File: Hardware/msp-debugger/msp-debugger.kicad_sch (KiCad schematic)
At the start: 22 parts, among them J1 Conn_02x10, J1 USB_B_Micro, J2 Conn_02x10, J4 Conn_01x04_Pin, SW1 222ADVBA, SW2 222ADVBA, SW3 222ADVBA, SW4 222ADVBA, SW5 222ADVBA, U1 MSP430G2553IN20, U3 BA033CC0FP-E2, U4 FT230XS-R

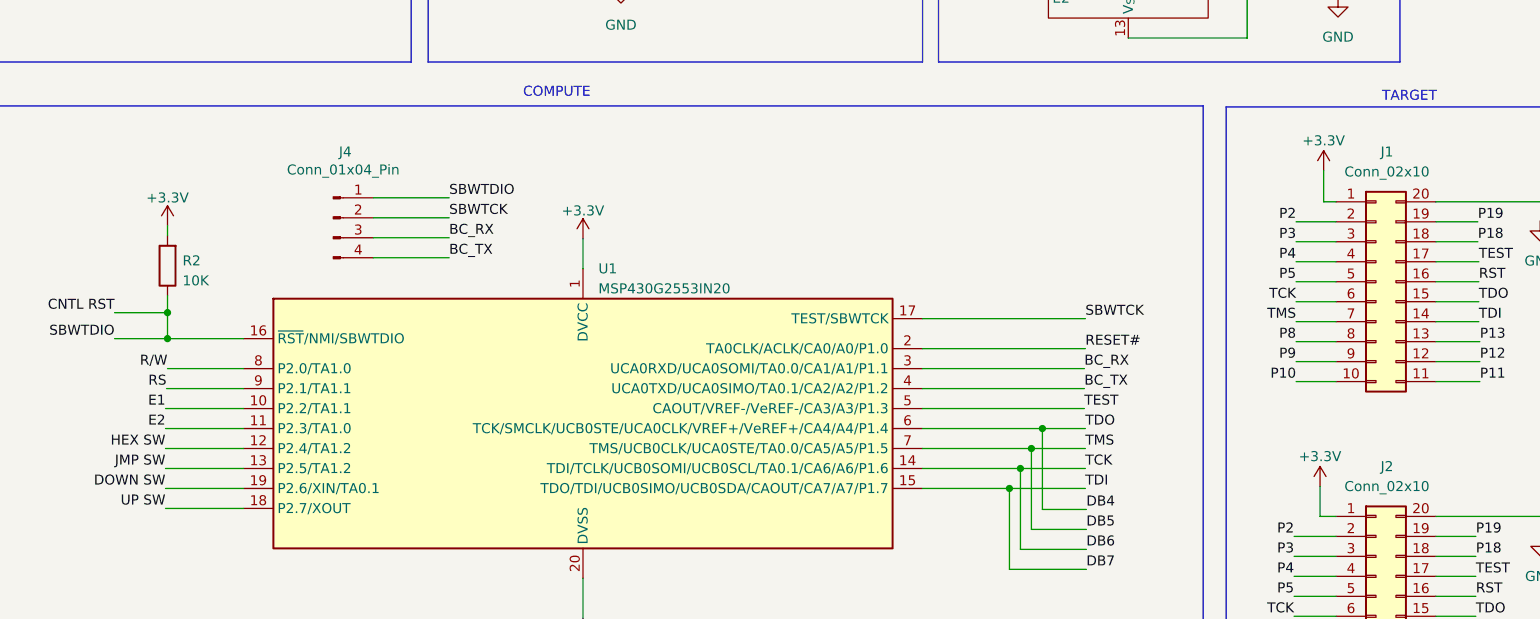
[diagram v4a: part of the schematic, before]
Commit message: reroute pcb for 40 line lcd screen
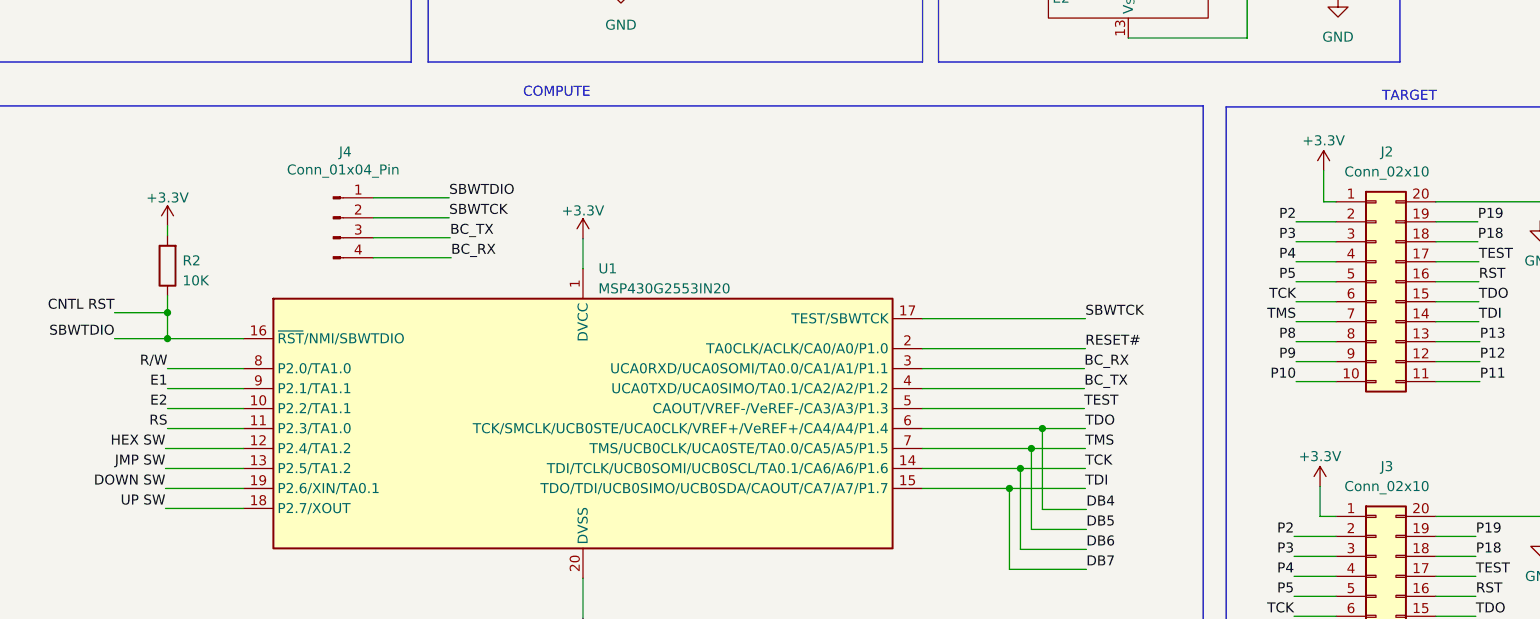
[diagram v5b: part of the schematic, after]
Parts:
- U2: footprint (none) -> project:NHD-0440AZ-FL-YBW
- VR1: footprint 3362P-1-103LF:TRIM_3362P-1-103LF -> project:TRIM_3362P-1-103LF
- renumbered J1 to J2, J2 to J3
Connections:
- net BC_RX: now also J4.4 (Pin_4); no longer J4.3 (Pin_3)
- net BC_TX: now also J4.3 (Pin_3); no longer J4.4 (Pin_4)
- net E1: now also U1.9 (P2.1/TA1.1); no longer U1.10 (P2.2/TA1.1)
- net E2: now also U1.10 (P2.2/TA1.1); no longer U1.11 (P2.3/TA1.0)
- net RS: now also U1.11 (P2.3/TA1.0); no longer U1.9 (P2.1/TA1.1)
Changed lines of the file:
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@@
+    (stroke (width 0) (type default))
+  )
+  (wire (pts (xy 124.968 101.6) (xy 134.874 101.6))
     (stroke (width 0) (type default))
   )
@@
     (stroke (width 0) (type default))
   )
-  (wire (pts (xy 124.968 99.06) (xy 134.62 99.06))
-    (stroke (width 0) (type default))
-  )
   (wire (pts (xy 233.68 64.77) (xy 236.093 64.77))
     (stroke (width 0) (type default))
@@
     (stroke (width 0) (type default))
   )
-  (wire (pts (xy 108.458 123.317) (xy 98.552 123.317))
-    (stroke (width 0) (type default))
-  )
   (wire (pts (xy 59.055 60.833) (xy 68.6054 60.833))
     (stroke (width 0) (type default))
@@
     (stroke (width 0) (type default))
   )
-  (wire (pts (xy 124.968 101.6) (xy 134.62 101.6))
-    (stroke (width 0) (type default))
-  )
   (wire (pts (xy 98.552 125.857) (xy 108.458 125.857))
     (stroke (width 0) (type default))
@@
     (stroke (width 0) (type default))
   )
+  (wire (pts (xy 108.458 120.777) (xy 98.806 120.777))
+    (stroke (width 0) (type default))
+  )
   (wire (pts (xy 54.483 109.601) (xy 56.388 109.601))
     (stroke (width 0) (type default))
   )
+  (wire (pts (xy 242.316 104.648) (xy 247.396 104.648))
+    (stroke (width 0) (type default))
+  )
   (wire (pts (xy 260.096 149.733) (xy 265.176 149.733))
     (stroke (width 0) (type default))
@@
     (stroke (width 0) (type default))
   )
+  (wire (pts (xy 98.806 118.237) (xy 108.458 118.237))
+    (stroke (width 0) (type default))
+  )
   (wire (pts (xy 203.0476 53.34) (xy 208.28 53.34))
     (stroke (width 0) (type default))
@@
     (stroke (width 0) (type default))
   )
-  (wire (pts (xy 242.316 104.648) (xy 247.396 104.648))
-    (stroke (width 0) (type default))
-  )
   (wire (pts (xy 151.638 142.367) (xy 151.638 147.447))
     (stroke (width 0) (type default))
@@
     (stroke (width 0) (type default))
   )
-  (wire (pts (xy 98.552 120.777) (xy 108.458 120.777))
-    (stroke (width 0) (type default))
-  )
   (wire (pts (xy 219.71 29.718) (xy 247.65 29.718))
     (stroke (width 0) (type default))
@@
     (stroke (width 0) (type default))
   )
-  (wire (pts (xy 98.679 118.237) (xy 108.458 118.237))
-    (stroke (width 0) (type default))
-  )
   (wire (pts (xy 42.418 119.126) (xy 44.323 119.126))
     (stroke (width 0) (type default))
@@
     (stroke (width 0) (type default))
   )
+  (wire (pts (xy 124.968 99.06) (xy 134.747 99.06))
+    (stroke (width 0) (type default))
+  )
   (wire (pts (xy 72.136 47.117) (xy 77.724 47.117))
     (stroke (width 0) (type default))
@@
     (stroke (width 0) (type default))
   )
+  (wire (pts (xy 108.458 123.317) (xy 98.806 123.317))
+    (stroke (width 0) (type default))
+  )
   (wire (pts (xy 37.973 119.126) (xy 42.418 119.126))
     (stroke (width 0) (type default))
@@
     (effects (font (size 1.27 1.27)) (justify right bottom))
   )
-  (label "E2" (at 98.552 123.317 180) (fields_autoplaced)
+  (label "E2" (at 98.806 120.777 180) (fields_autoplaced)
     (effects (font (size 1.27 1.27)) (justify right bottom))
   )
@@
     (effects (font (size 1.27 1.27)) (justify right bottom))
   )
-  (label "BC_RX" (at 134.62 99.06 0) (fields_autoplaced)
+  (label "BC_RX" (at 134.874 101.6 0) (fields_autoplaced)
     (effects (font (size 1.27 1.27)) (justify left bottom))
   )
@@
     (effects (font (size 1.27 1.27)) (justify left bottom))
   )
-  (label "E1" (at 98.552 120.777 180) (fields_autoplaced)
+  (label "E1" (at 98.806 118.237 180) (fields_autoplaced)
     (effects (font (size 1.27 1.27)) (justify right bottom))
   )
@@
     (effects (font (size 1.27 1.27)) (justify right bottom))
   )
-  (label "RS" (at 98.679 118.237 180) (fields_autoplaced)
+  (label "RS" (at 98.806 123.317 180) (fields_autoplaced)
     (effects (font (size 1.27 1.27)) (justify right bottom))
   )
@@
     (effects (font (size 1.27 1.27)) (justify left bottom))
   )
-  (label "BC_TX" (at 134.62 101.6 0) (fields_autoplaced)
+  (label "BC_TX" (at 134.747 99.06 0) (fields_autoplaced)
     (effects (font (size 1.27 1.27)) (justify left bottom))
   )
@@
       (effects (font (size 1.27 1.27)) (justify left))
     )
-    (property "Footprint" "3362P-1-103LF:TRIM_3362P-1-103LF" (at 247.65 39.878 0)
+    (property "Footprint" "project:TRIM_3362P-1-103LF" (at 247.65 39.878 0)
       (effects (font (size 1.27 1.27)) (justify bottom) hide)
     )
@@
   (symbol (lib_id "Connector_Generic:Conn_02x10_Counter_Clockwise") (at 252.476 104.648 0) (unit 1)
     (in_bom yes) (on_board yes) (dnp no)
-    (property "Reference" "J1" (at 253.873 88.138 0)
+    (property "Reference" "J2" (at 253.873 88.138 0)
       (effects (font (size 1.27 1.27)))
     )
@@
       (project "msp-debugger"
         (path "/045ba461-bcb4-4373-9dc5-687bfd2826ef"
-          (reference "J1") (unit 1)
+          (reference "J2") (unit 1)
         )
       )
@@
       (effects (font (size 1.27 1.27)))
     )
-    (property "Footprint" "" (at 220.98 46.99 0)
+    (property "Footprint" "project:NHD-0440AZ-FL-YBW" (at 220.98 46.99 0)
       (effects (font (size 1.27 1.27)) hide)
     )
@@
   (symbol (lib_id "Connector_Generic:Conn_02x10_Counter_Clockwise") (at 252.476 144.653 0) (unit 1)
     (in_bom yes) (on_board yes) (dnp no)
-    (property "Reference" "J2" (at 253.873 128.143 0)
+    (property "Reference" "J3" (at 253.873 128.143 0)
       (effects (font (size 1.27 1.27)))
     )
@@
       (project "msp-debugger"
         (path "/045ba461-bcb4-4373-9dc5-687bfd2826ef"
-          (reference "J2") (unit 1)
-        )
-      )
+          (reference "J3") (unit 1)
+        )
+      )

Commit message: fix hardware issues and route small pcb
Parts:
- removed J3: Conn_02x10, Connector_PinHeader_2.54mm:PinHeader_2x10_P2.54mm_Vertical, symbol Connector_Generic:Conn_02x10_Counter_Clockwise
- removed J4: Conn_01x04_Pin, Connector_PinHeader_2.54mm:PinHeader_1x04_P2.54mm_Vertical, symbol Connector:Conn_01x04_Pin
- removed U4: FT230XS-R, digikey-footprints:SOIC-16_W3.90mm, symbol dk_Interface-Controllers:FT230XS-R
- added J4: MSP_FET PORT, Connector_PinHeader_2.54mm:PinHeader_2x03_P2.54mm_Vertical, symbol Connector_Generic:Conn_02x03_Counter_Clockwise
- added J5: USB JUMPER, Connector_PinHeader_2.54mm:PinHeader_2x03_P2.54mm_Vertical, symbol Connector_Generic:Conn_02x03_Counter_Clockwise
- added J6, J7: Conn_01x10, Connector_PinHeader_2.54mm:PinHeader_1x10_P2.54mm_Vertical, symbol Connector_Generic:Conn_01x10
- added R10, R3, R4, R5, R6, R7, R8, R9: 10K, Capacitor_SMD:C_0805_2012Metric, symbol Device:R
- added SW6: 222ADVBA, buttons:SW_222ADVBA, symbol Switch:SW_MEC_5E
- added U4: FT230XS-R, SOIC_30XS-R_FTD, symbol ft230xs-r:FT230XS-R
- added U5, U6, U7, U8: AO4882, SO-8_AOS, symbol ao4882:AO4882
- J1: footprint Connector_USB:USB_Micro-B_Amphenol_10118194_Horizontal -> Connector_PinHeader_2.54mm:PinHeader_1x05_P2.54mm_Vertical
- U2: footprint project:NHD-0440AZ-FL-YBW -> Connector_PinHeader_2.54mm:PinHeader_2x09_P2.54mm_Vertical
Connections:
- net RST is gone; now on net DB7: J2.16 (Pin_16)
- net +3.3V: now also J6.1 (Pin_1), U4.3 (VCCIO)
- net +5V: now also U4.12 (VCC), U5.5 (D1), U5.6 (D1), U5.7 (D2), U5.8 (D2), U6.5 (D1), U6.6 (D1), U6.7 (D2), U6.8 (D2), U7.5 (D1), U7.6 (D1), U7.7 (D2), U7.8 (D2), U8.5 (D1), U8.6 (D1), U8.7 (D2), U8.8 (D2)
- net BC_RX: now also J4.5 (Pin_5), J5.5 (Pin_5)
- net BC_TX: now also J4.6 (Pin_6), J5.4 (Pin_4)
- net CNTL RST: now also J4.3 (Pin_3)
- net D+: now also U4.8 (USBDP)
- net D-: now also U4.9 (USBDM)
- net DB4: now also J2.14 (Pin_14), U1.7 (TMS/UCB0CLK/UCA0STE/TA0.0/CA5/A5/P1.5), J7.4 (Pin_4), U5.4 (G1); no longer J2.15 (Pin_15), U1.6 (TCK/SMCLK/UCB0STE/UCA0CLK/VREF+/VeREF+/CA4/A4/P1.4), U2.4 (DB4)
- net DB5: now also J2.17 (Pin_17), U1.2 (TA0CLK/ACLK/CA0/A0/P1.0), J7.7 (Pin_7), U6.2 (G2); no longer J2.7 (Pin_7), U1.7 (TMS/UCB0CLK/UCA0STE/TA0.0/CA5/A5/P1.5), U2.3 (DB5)
- net DB6: now also J2.15 (Pin_15), U1.6 (TCK/SMCLK/UCB0STE/UCA0CLK/VREF+/VeREF+/CA4/A4/P1.4), J7.5 (Pin_5), U5.2 (G2); no longer J2.6 (Pin_6), U1.14 (TDI/TCLK/UCB0SOMI/UCB0SCL/TA0.1/CA6/A6/P1.6), U2.2 (DB6)
- net DB7: now also U1.5 (CAOUT/VREF-/VeREF-/CA3/A3/P1.3), J7.6 (Pin_6), U6.4 (G1); no longer J2.14 (Pin_14), U1.15 (TDO/TDI/UCB0SIMO/UCB0SDA/CAOUT/CA7/A7/P1.7), U2.1 (DB7)
- net DOWN SW: now also U1.18 (P2.7/XOUT); no longer U1.19 (P2.6/XIN/TA0.1)
- net E1: now also U1.11 (P2.3/TA1.0), U7.4 (G1); no longer U1.9 (P2.1/TA1.1), U2.9 (E1)
- net E2: now also U1.9 (P2.1/TA1.1), U8.4 (G1); no longer U1.10 (P2.2/TA1.1), U2.15 (E2)
- net GND: now also J4.2 (Pin_2), J7.10 (Pin_10), R10.1, R3.1, R4.1, R5.1, R6.1, R7.1, R8.1, R9.1, SW6.1, SW6.2, U4.13 (GND), U4.5 (GND)
- net P10: now also J6.10 (Pin_10)
- net P11: now also J7.1 (Pin_1)
- net P12: now also J7.2 (Pin_2)
- net P13: now also J7.3 (Pin_3)
- net P18: now also J7.8 (Pin_8)
- net P19: now also J7.9 (Pin_9)
- net P2: now also J6.2 (Pin_2)
- net P3: now also J6.3 (Pin_3)
- net P4: now also J6.4 (Pin_4)
- net P5: now also J6.5 (Pin_5)
- net P8: now also J6.8 (Pin_8)
- net P9: now also J6.9 (Pin_9)
- net RESET#: now also SW6.3 (K), SW6.4 (A), U4.11 (RESET#); no longer U1.2 (TA0CLK/ACLK/CA0/A0/P1.0)
- net RS: now also U1.10 (P2.2/TA1.1), U7.2 (G2); no longer U1.11 (P2.3/TA1.0), U2.11 (RS)
- net R/W: now also U8.2 (G2); no longer U2.10 (R/W)
- net SBWTCK: now also J4.4 (Pin_4)
- net UP SW: now also U1.19 (P2.6/XIN/TA0.1); no longer U1.18 (P2.7/XOUT)
- net PWR_IN: now reaches F1.1
- net PWR_IN: now also J4.1 (Pin_1), J5.6 (Pin_6); no longer J1.1 (VBUS)
- removed net TEST: J2.17 (Pin_17), U1.5 (CAOUT/VREF-/VeREF-/CA3/A3/P1.3)
- new net BRIDGE_RX: J5.2 (Pin_2), U4.4 (RXD)
- new net BRIDGE_TX: J5.3 (Pin_3), U4.1 (TXD)
- new net DB4_5V: R4.2, U2.4 (DB4), U5.3 (S1)
- new net DB5_5V: R7.2, U2.3 (DB5), U6.1 (S2)
- new net DB6_5V: R3.2, U2.2 (DB6), U5.1 (S2)
- new net DB7_5V: R8.2, U2.1 (DB7), U6.3 (S1)
- new net E1_5V: R6.2, U2.9 (E1), U7.3 (S1)
- new net E2_5V: R10.2, U2.15 (E2), U8.3 (S1)
- new net RS_5V: R5.2, U2.11 (RS), U7.1 (S2)
- new net R/W_5V: R9.2, U2.10 (R/W), U8.1 (S2)
- new net TCK: J2.6 (Pin_6), J6.6 (Pin_6), U1.15 (TDO/TDI/UCB0SIMO/UCB0SDA/CAOUT/CA7/A7/P1.7)
- new net TMS: J2.7 (Pin_7), J6.7 (Pin_7), U1.14 (TDI/TCLK/UCB0SOMI/UCB0SCL/TA0.1/CA6/A6/P1.6)
- new net USB_IN: J1.1 (VBUS), J5.1 (Pin_1)
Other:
- note added: "DATA LINE SWITCHES"
- moved on the sheet: C1, C2, C3, C4, D1, F1, J1, J2, R1, R2, SW1, SW2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
